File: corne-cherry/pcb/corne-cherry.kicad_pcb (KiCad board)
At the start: 2 copper layers, 275.5 x 105.6 mm, 172 parts, among them SW1 SW_PUSH, SW10 SW_PUSH, SW11 SW_PUSH, SW12 SW_PUSH, SW13 SW_PUSH, SW14 SW_PUSH, SW15 SW_PUSH, SW16 SW_PUSH, SW17 SW_PUSH, SW18 SW_PUSH, SW19 SW_PUSH, SW2 SW_PUSH, SW20 SW_PUSH, SW21 SW_PUSH, SW22 SW_PUSH, SW23 SW_PUSH, SW24 SW_PUSH, SW25 SW_PUSH, SW26 SW_PUSH, SW27 SW_PUSH, SW28 SW_PUSH, SW29 SW_PUSH, SW3 SW_PUSH, SW30 SW_PUSH, SW31 SW_PUSH, SW32 SW_PUSH, SW33 SW_PUSH, SW34 SW_PUSH, SW35 SW_PUSH, SW36 SW_PUSH, SW37 SW_PUSH, SW38 SW_PUSH, SW39 SW_PUSH, SW4 SW_PUSH, SW40 SW_PUSH, SW41 SW_PUSH, SW42 SW_PUSH, SW5 SW_PUSH, SW6 SW_PUSH, SW7 SW_PUSH, SW8 SW_PUSH, SW9 SW_PUSH, U1 nice_nano

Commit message: minor improvements in tracing
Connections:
- U1 pad 23: (no net) -> GND
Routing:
- net reset: track 58.3 -> 43.8 mm
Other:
- rule pad_to_mask_clearance: 0.2 -> 0
- board text added: "+"
- board text added: "-"
- board text added: "OFF"
- board text added: "ON"

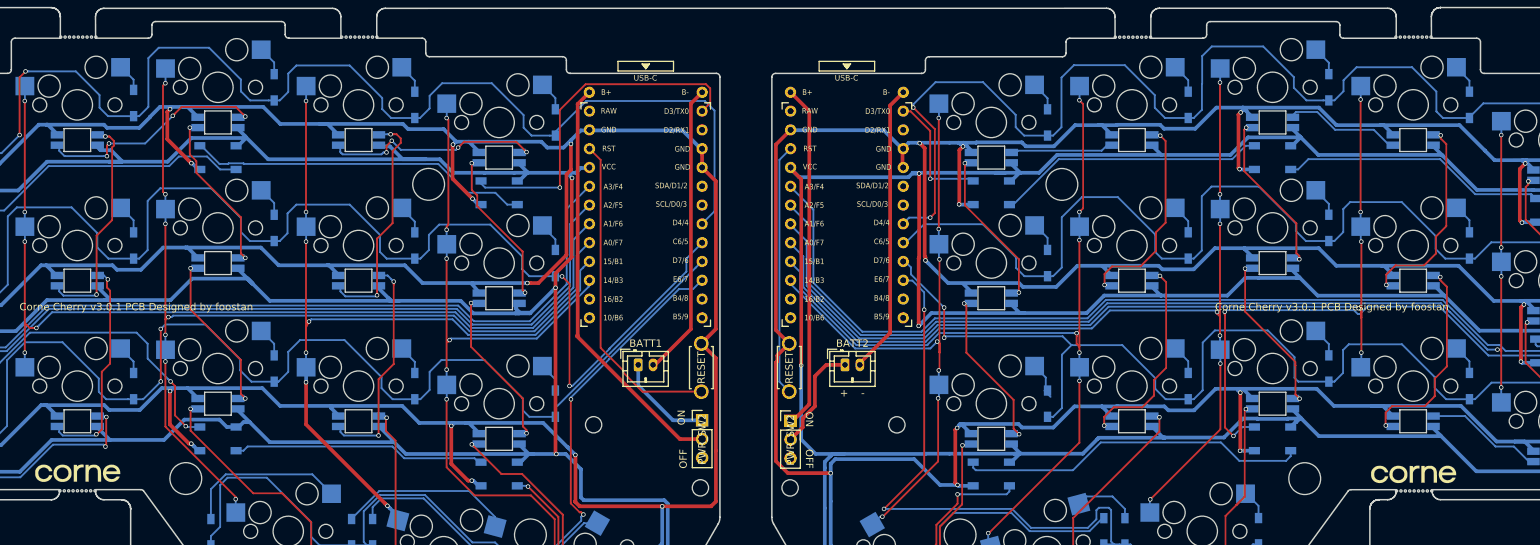
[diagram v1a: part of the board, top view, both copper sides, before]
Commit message: added support for tenting puck
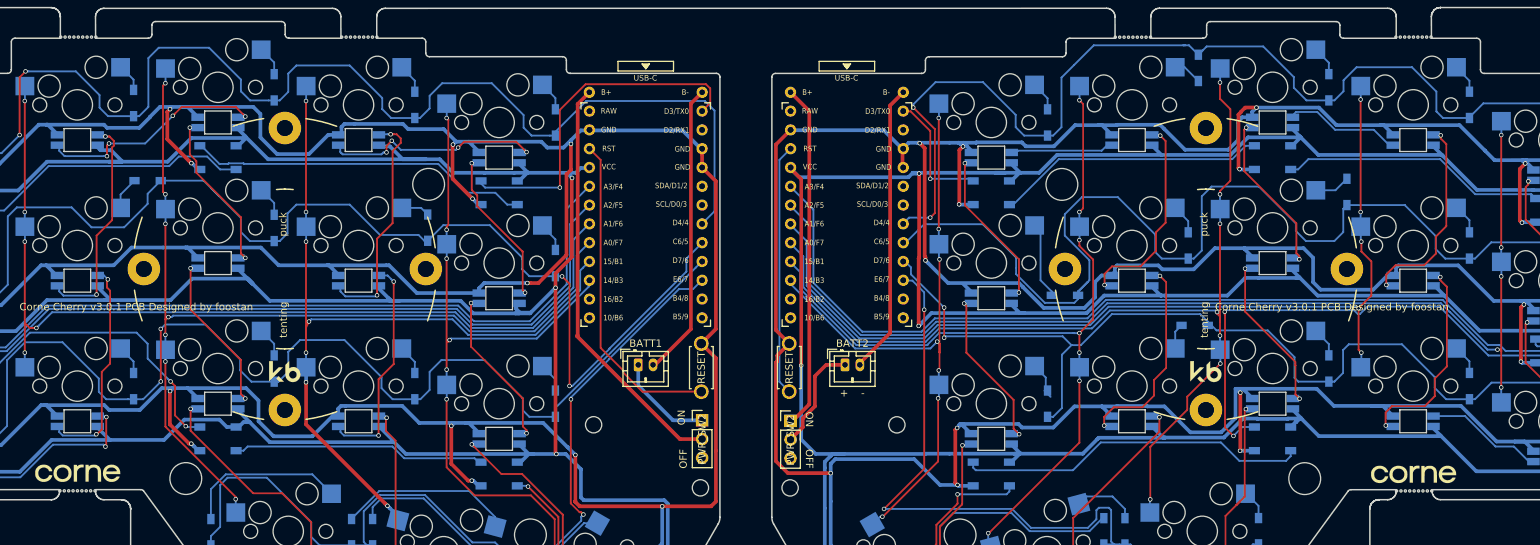
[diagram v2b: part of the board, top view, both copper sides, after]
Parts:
- added REF**: Tenting Puck, kbd:Tenting_Puck, F.Cu at (86.1, 53.2)
- added REF**: Tenting Puck, kbd:Tenting_Puck, F.Cu at (210.6, 53.2)
- moved D9 8.97 mm to (67.6, 41.3), turned to 180 degrees
- moved D38 8.24 mm to (209.1, 60.8), turned to 180 degrees
- moved D31 5.44 mm to (229.7, 42.8)
- moved D26 5.18 mm to (209.6, 26.0), turned to 270 degrees
- moved D33 4.95 mm to (191.6, 56.8), turned to 180 degrees
- moved D11 2.98 mm to (105.5, 47.6)
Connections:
- U1 pad 16: (no net) -> col4_r
- U1 pad 8: (no net) -> row1_r
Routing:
- net GNDA: track 605.2 -> 619.1 mm
- net row1_r: track 166.9 -> 179.4 mm
- net row1: track 188.6 -> 178.5 mm
- net row0_r: track 184.4 -> 175.4 mm
- net row2_r: track 172.6 -> 164.1 mm
- net Net-(D33-Pad2): track 4.08 -> 10.5 mm
- net GND: track 634.1 -> 639.7 mm
- net col3_r: track 133.0 -> 134.1 mm
- net Net-(D31-Pad2): track 4.03 -> 4.84 mm
- net (no net): track 209.6 -> 210.4 mm
- net Net-(D38-Pad2): track 4.05 -> 3.47 mm

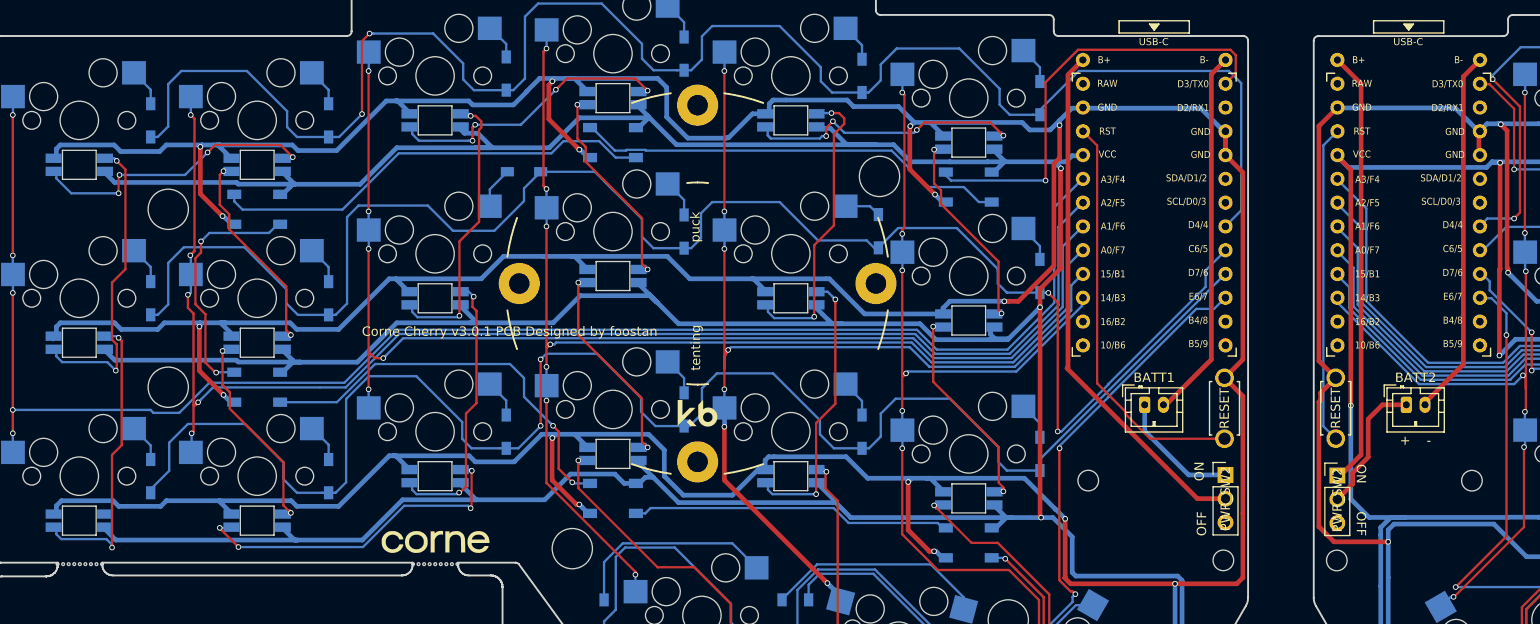
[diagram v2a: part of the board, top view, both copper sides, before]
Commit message: added support for tenting puck in bottom plate
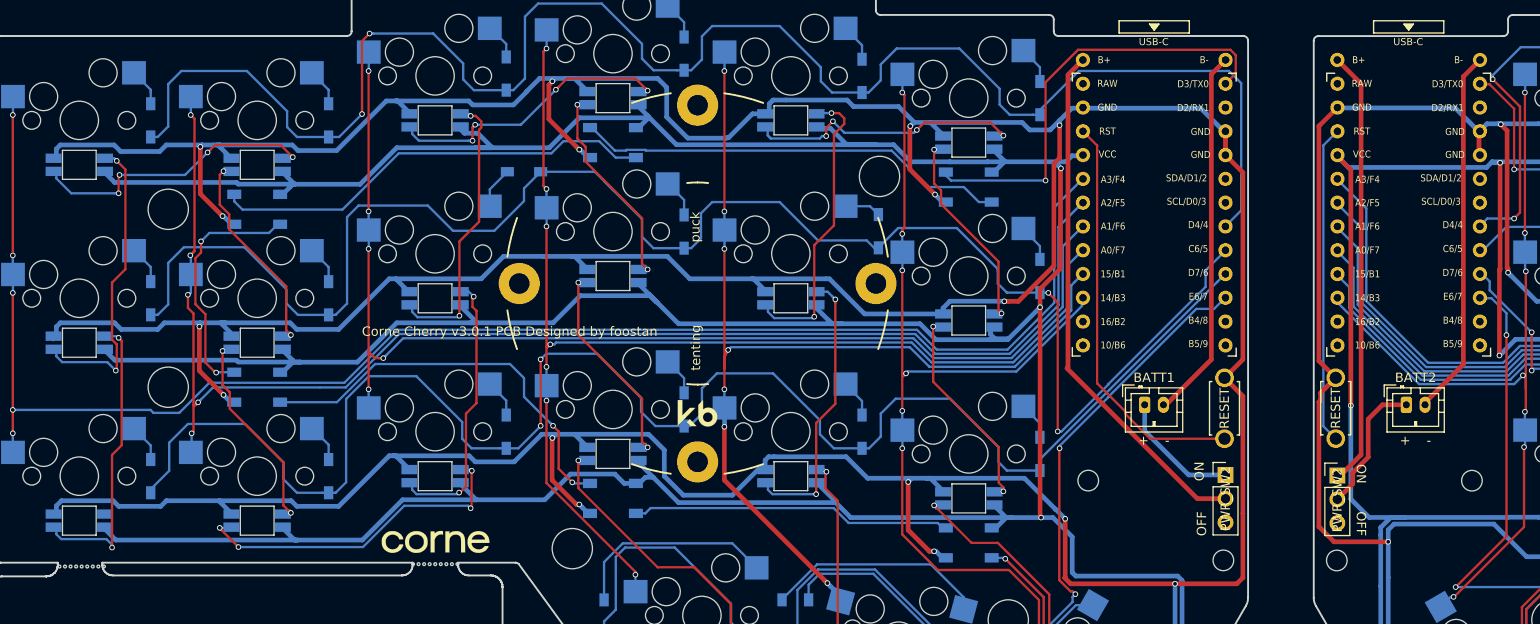
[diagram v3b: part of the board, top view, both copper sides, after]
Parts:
- moved REF** 0.32 mm to (20.4, 83.4)

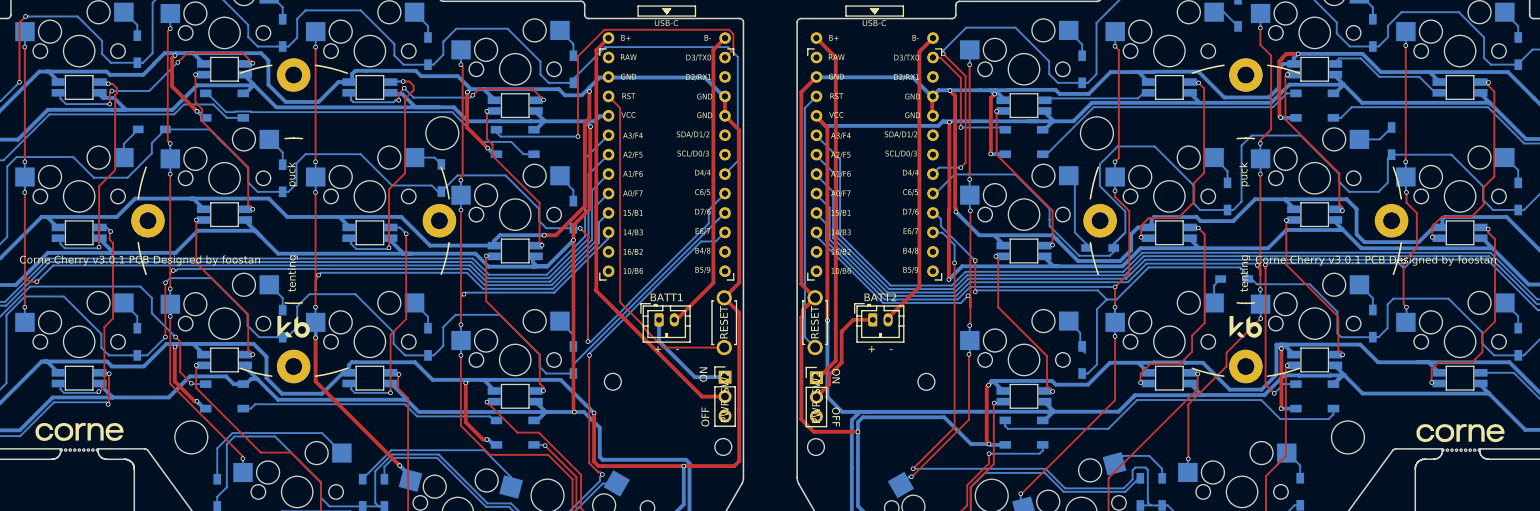
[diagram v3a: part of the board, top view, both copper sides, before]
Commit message: adjusted position of tenting puck to match switch cut outs in top plate of case
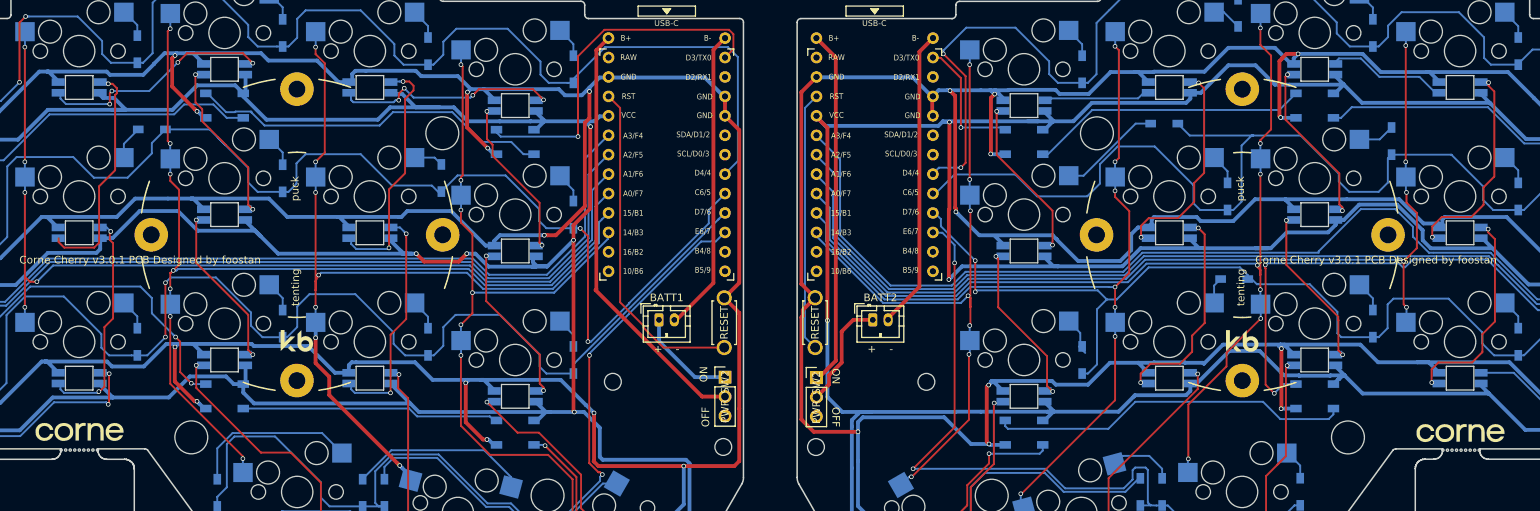
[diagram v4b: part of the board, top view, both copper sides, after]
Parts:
- moved D33 18.3 mm to (199.9, 40.5)
- moved REF** 1.91 mm to (210.1, 55.1)
- moved REF** 1.89 mm to (86.6, 55.0)
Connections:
- U1 pad 15: (no net) -> col5
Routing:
- net GNDA: track 619.1 -> 608.2 mm
- net row1_r: track 179.4 -> 170.3 mm
- net GND: track 639.7 -> 632.5 mm
- net col0_r: track 175.8 -> 181.4 mm
- net VDD: track 568.9 -> 573.7 mm
- net Net-(D33-Pad2): track 10.5 -> 13.6 mm
- net VCC: track 518.8 -> 520.8 mm, vias 3 -> 5
- net Net-(LED2-Pad4): track 46.3 -> 47.8 mm
- net col4: track 110.4 -> 111.4 mm
- net Net-(LED15-Pad4): track 30.8 -> 30.3 mm, vias 2 -> 1
